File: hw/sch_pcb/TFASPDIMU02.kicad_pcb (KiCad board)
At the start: 2 copper layers, 30 x 15 mm, 39 parts, among them J1 SM04B-GHS-TB, M1 HOLE_TF, M2 HOLE_TF, M3 HOLE_TF, M7 HOLE_TF, U1 SDP3x, U2 ICM-20948, U3 TCA9617A, U4 MIC5504-3.3YM5-TR, U5 MIC5504-1.8YM5-TR, U6 TCA9617A

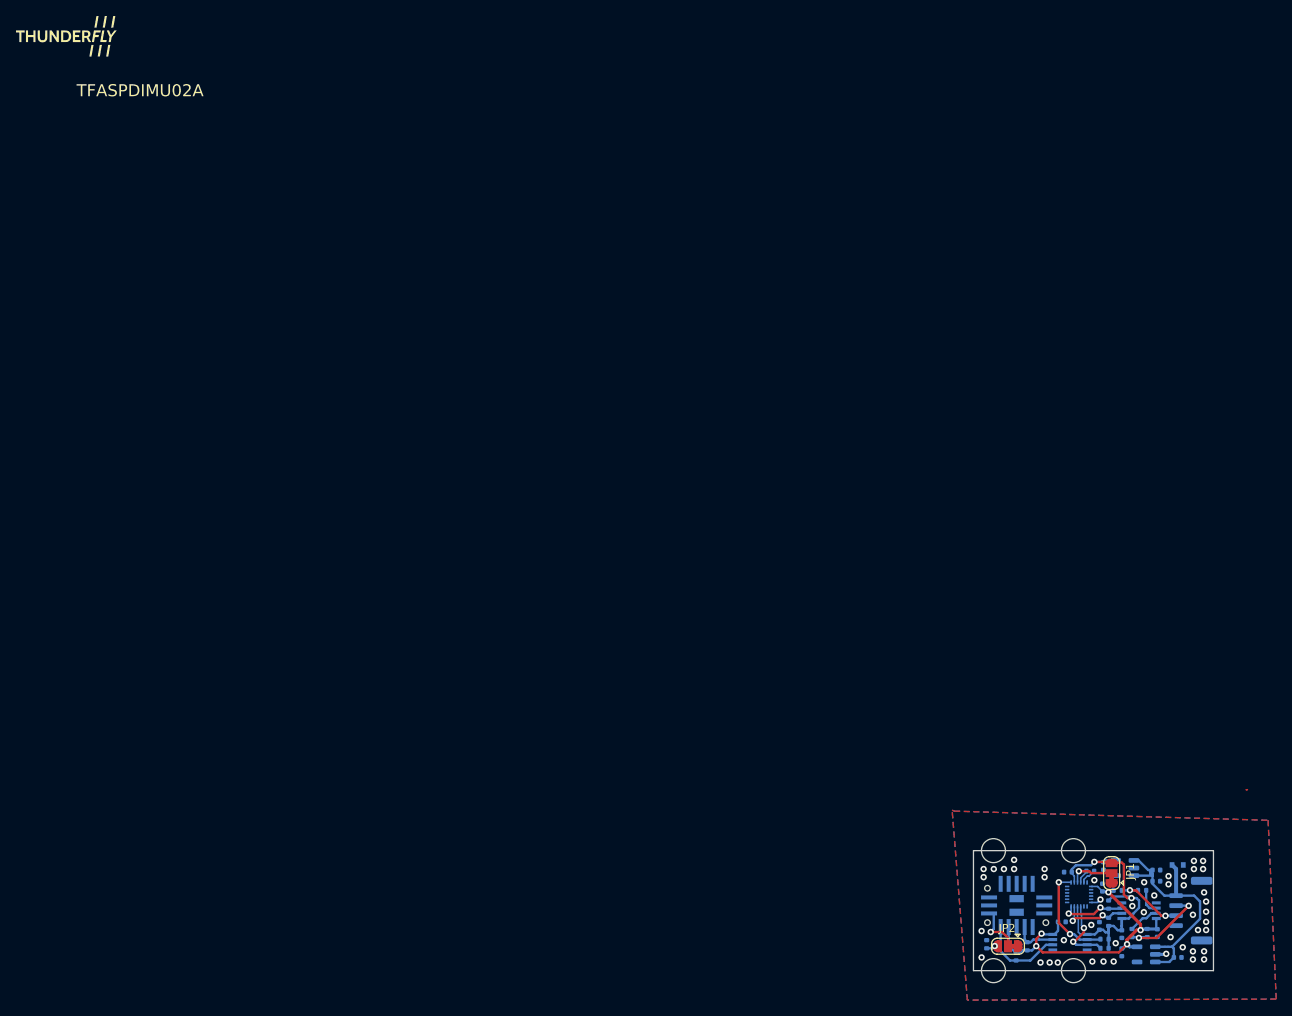
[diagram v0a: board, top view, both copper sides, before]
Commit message: Improved layout.
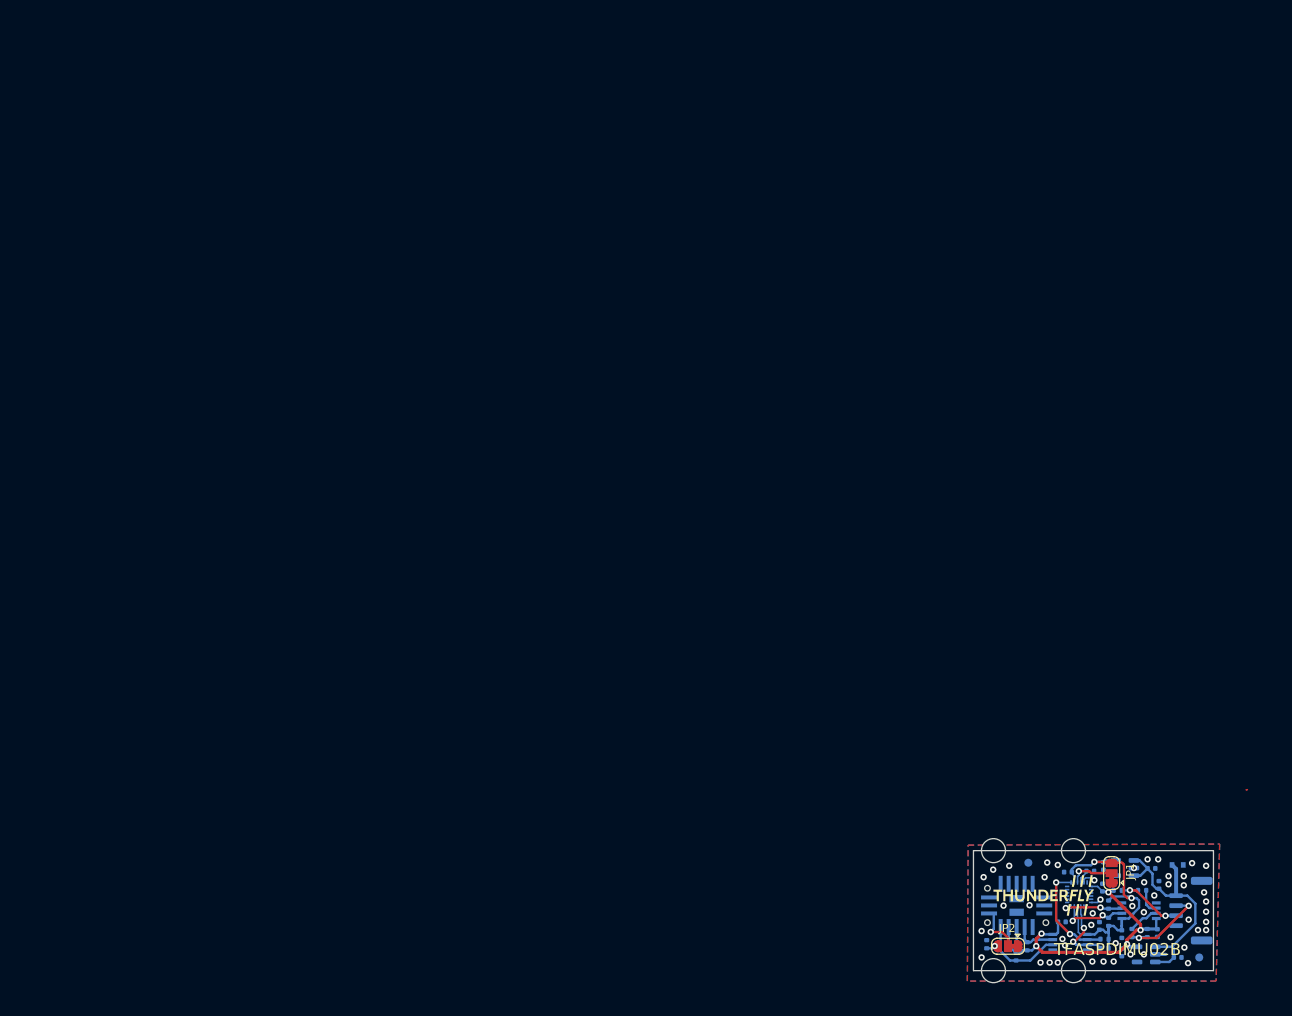
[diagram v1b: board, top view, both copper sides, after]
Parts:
- added FID1: Fiducial, Fiducial:Fiducial_1mm_Mask2mm, B.Cu at (128.5, 94.2)
- added FID2: Fiducial, Fiducial:Fiducial_1mm_Mask2mm, B.Cu at (149.9, 106.0)
- R10: value 1k2 -> 2k7
- R2, R3: value 1k5 -> 2k7
- R4, R5, R6, R7, R8, R9: value 1k5 -> 10k
- moved G*** 162.7 mm to (130.4, 98.3)
- moved C6 0.64 mm to (143.9, 94.9)
- moved C11 0.56 mm to (144.9, 97.0), turned to 90 degrees
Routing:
- net GND: track 5.05 -> 6.86 mm, vias 47 -> 48
- net +5V: track 31.7 -> 30.1 mm
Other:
- board text added: "TFASPDIMU02B"
- board text removed: "TFASPDIMU02A"

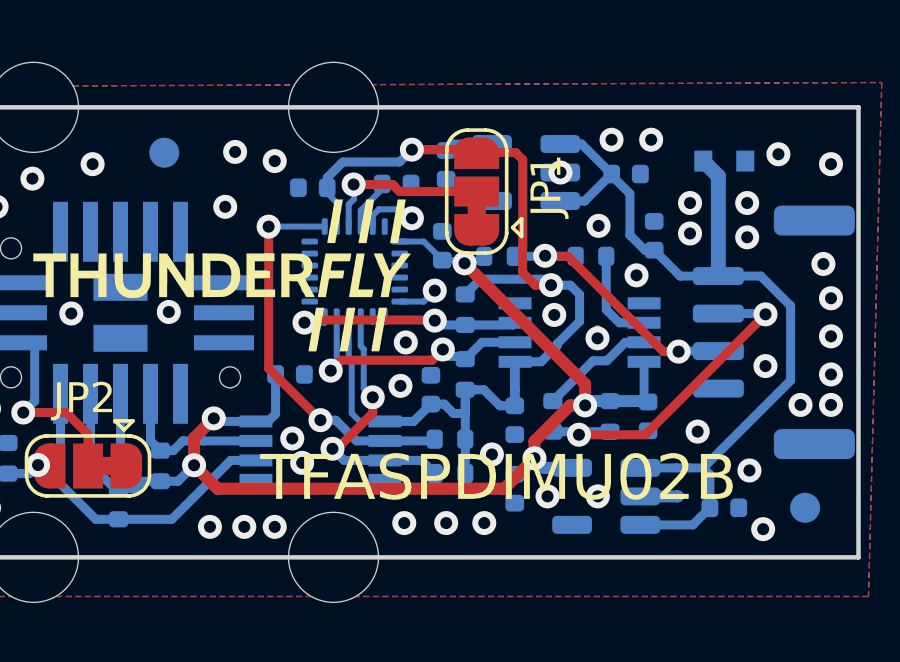
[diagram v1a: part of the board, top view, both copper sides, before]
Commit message: footprint of translator changed to VSSOP.
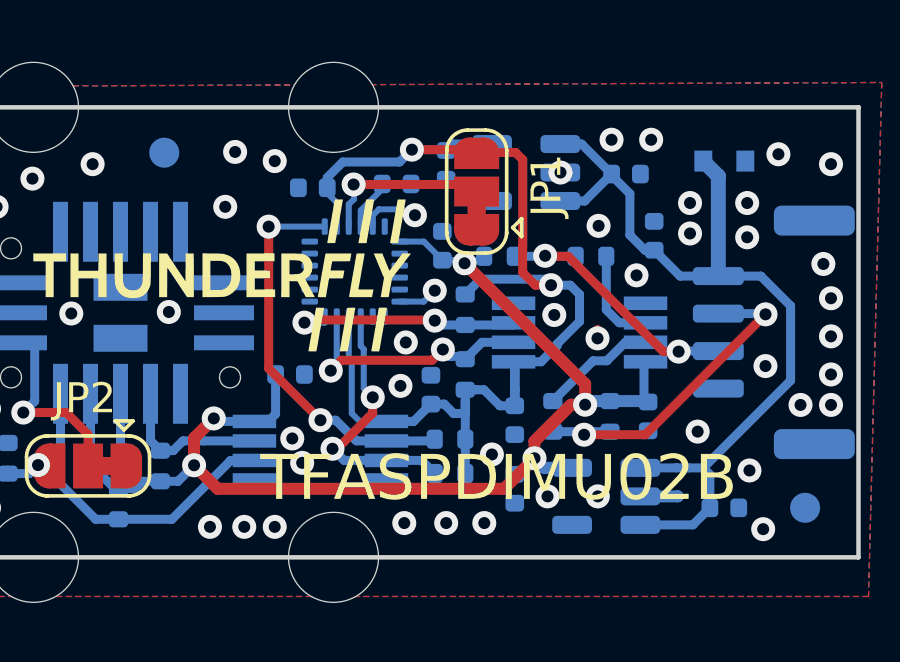
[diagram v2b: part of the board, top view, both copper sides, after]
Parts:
- U3, U6: footprint Package_SO:TSSOP-8_3x3mm_P0.65mm -> Package_SO:VSSOP-8_3.0x3.0mm_P0.65mm
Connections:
- net +3V3 renamed +3.3V

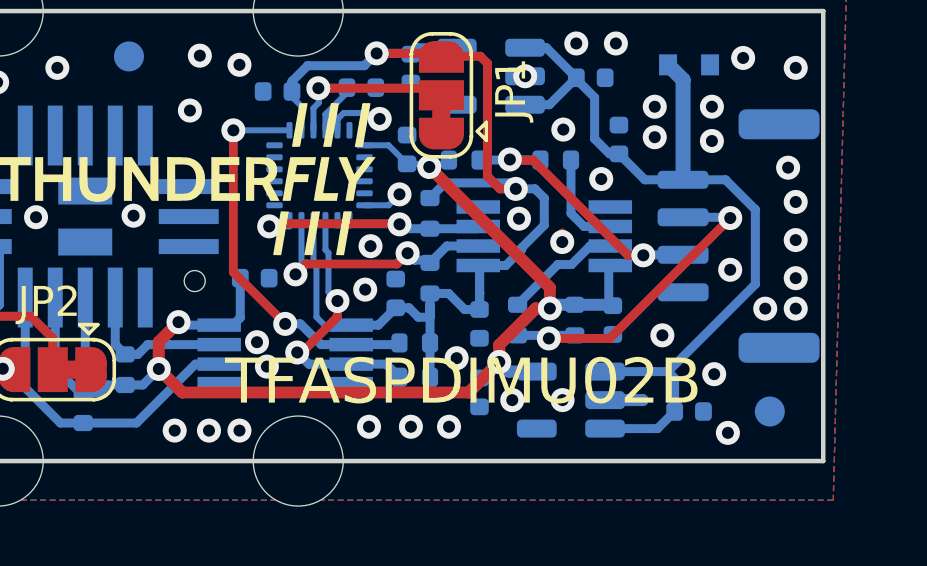
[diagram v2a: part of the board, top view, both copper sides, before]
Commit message: Revert TSSOP footprint.
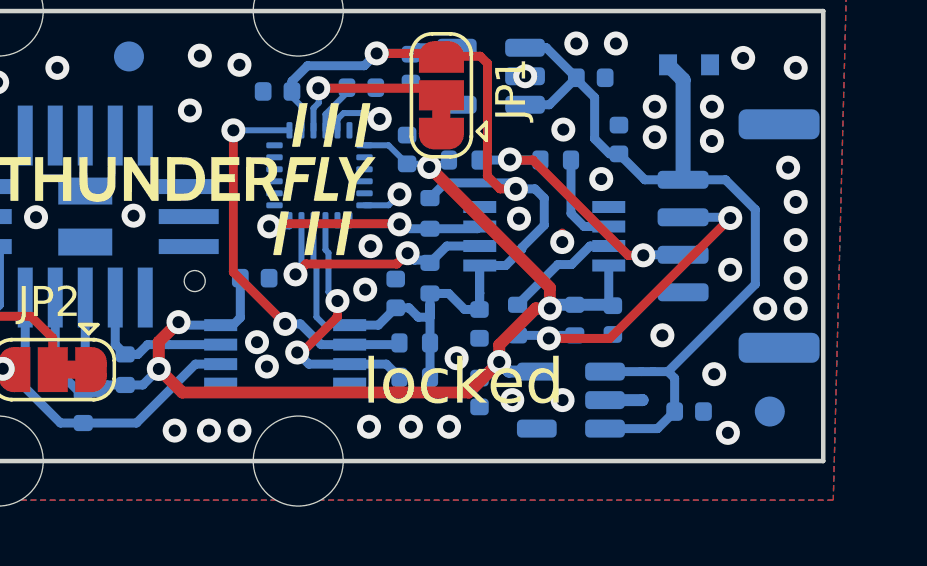
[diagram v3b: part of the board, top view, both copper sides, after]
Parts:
- U3, U6: value TCA9617A -> PCA9617A; footprint Package_SO:VSSOP-8_3.0x3.0mm_P0.65mm -> Package_SO:TSSOP-8_3x3mm_P0.65mm
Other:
- board text added: "locked"
- board text removed: "TFASPDIMU02B"

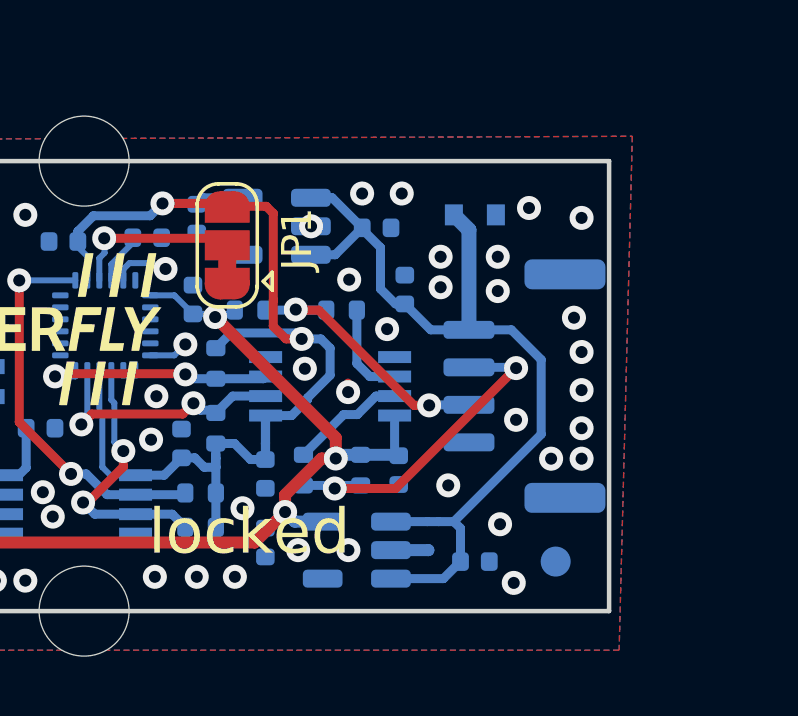
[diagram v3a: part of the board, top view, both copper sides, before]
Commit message: Implement power indicating LED.
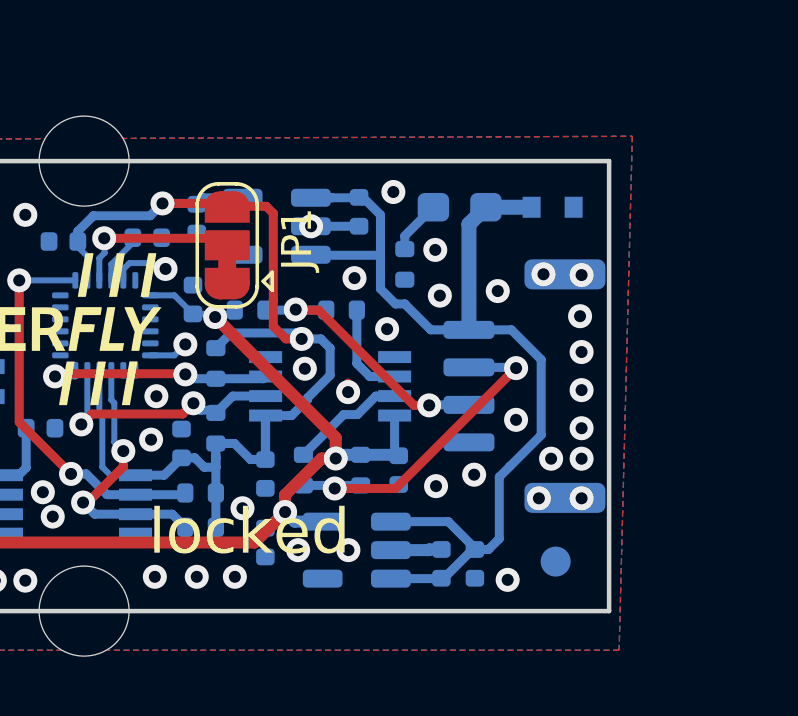
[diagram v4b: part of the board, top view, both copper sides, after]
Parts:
- added D1: GREEN, LED_SMD:LED_0603_1608Metric_Pad1.05x0.95mm_HandSolder, B.Cu at (146.7, 94.2)
- added R12: 180R, Resistor_SMD:R_0402_1005Metric, B.Cu at (144.9, 96.1)
- moved C11 9.44 mm to (147.2, 106.1), turned to -90 degrees
- moved D2 2.60 mm to (149.8, 94.2)
- moved C5 1.12 mm to (146.1, 106.1), turned to 90 degrees
- moved C6 0.79 mm to (143.3, 94.4), turned to -90 degrees
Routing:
- net +5V: track 30.1 -> 35.0 mm
- net GND: track 6.86 -> 8.98 mm
- net Net-(D1-K): track 0.00 -> 1.79 mm

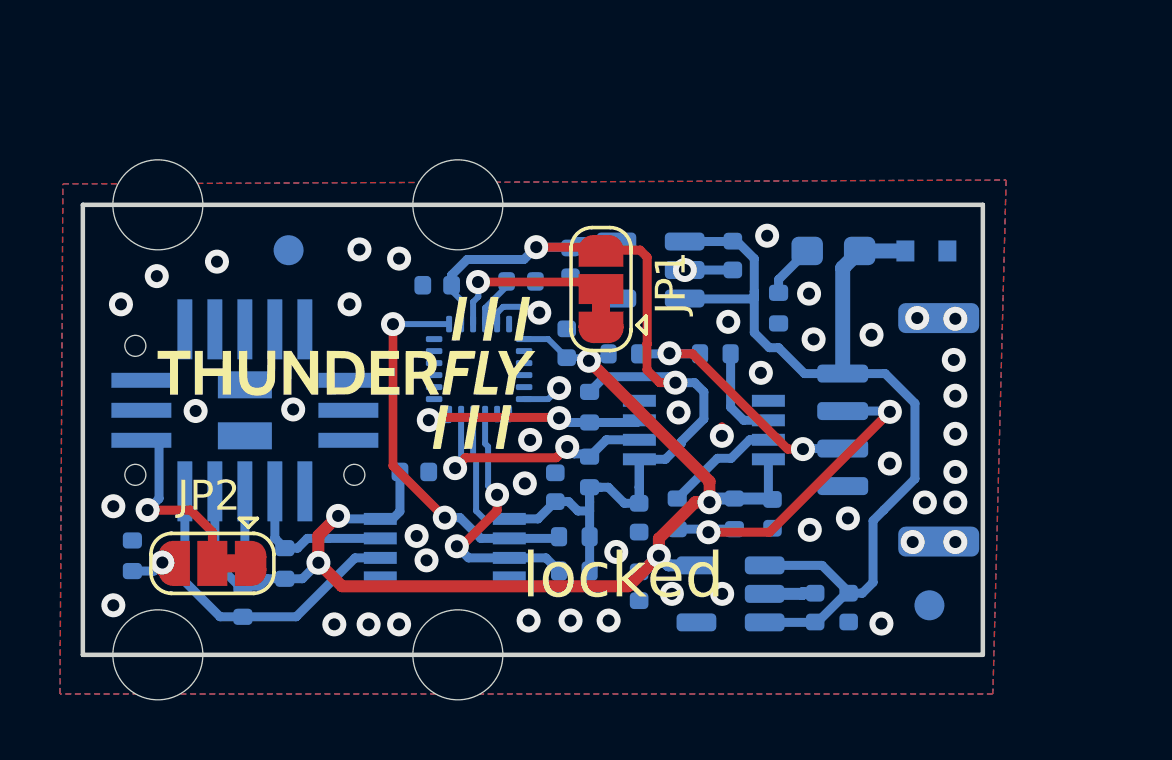
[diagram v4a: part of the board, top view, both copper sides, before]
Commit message: Update footprints from library. Improve layout Move I2C connector inside to PCB to meet manufacturing limits.
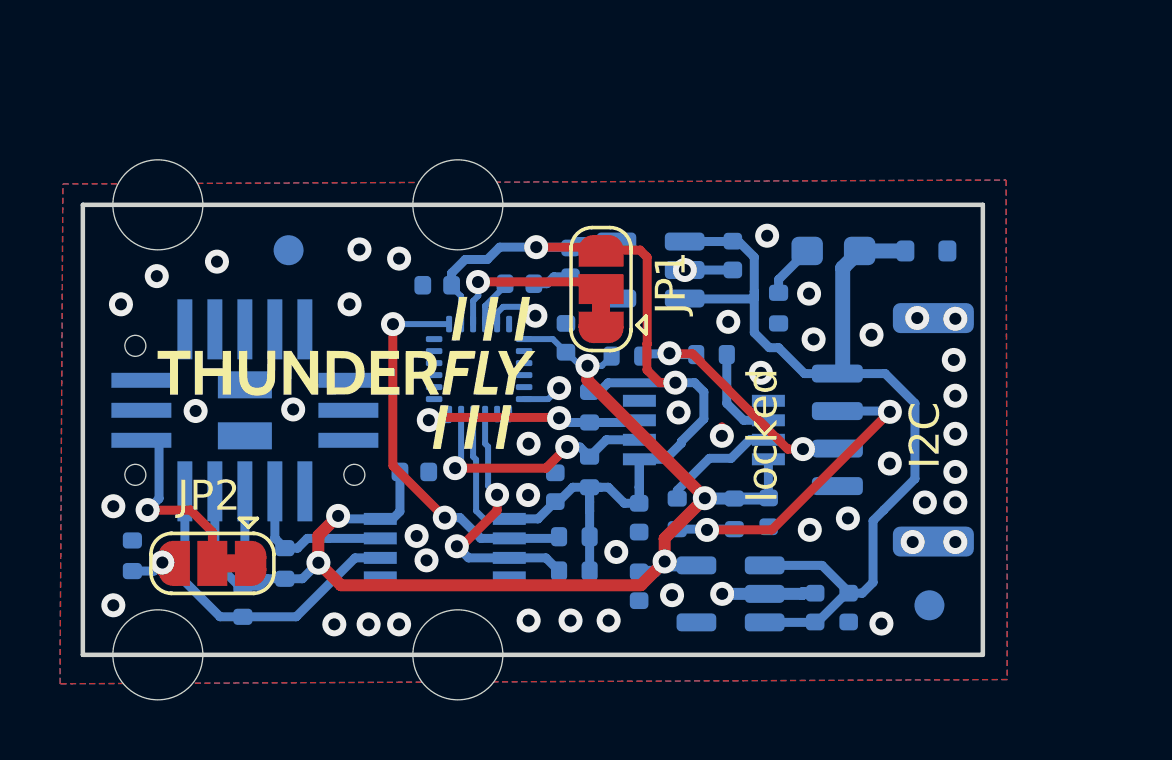
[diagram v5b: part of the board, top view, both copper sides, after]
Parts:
- moved C3 0.18 mm to (137.8, 97.1)
- moved J1 0.18 mm to (148.7, 100.2)
- moved C13 0.14 mm to (144.5, 102.9)
- moved R11 0.13 mm to (142.6, 97.7)
- moved R3 0.13 mm to (139.8, 97.7)
- moved C4 0.09 mm to (136.2, 95.3)
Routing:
- net GND: track 8.98 -> 11.7 mm
- net +3.3V: track 42.8 -> 41.7 mm
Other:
- rule pad_to_mask_clearance: 0.2 -> 0.05
- board text added: "I2C"
